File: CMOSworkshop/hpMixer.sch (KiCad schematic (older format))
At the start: 22 parts, among them J1 JACK_STEREO, U4 TL082

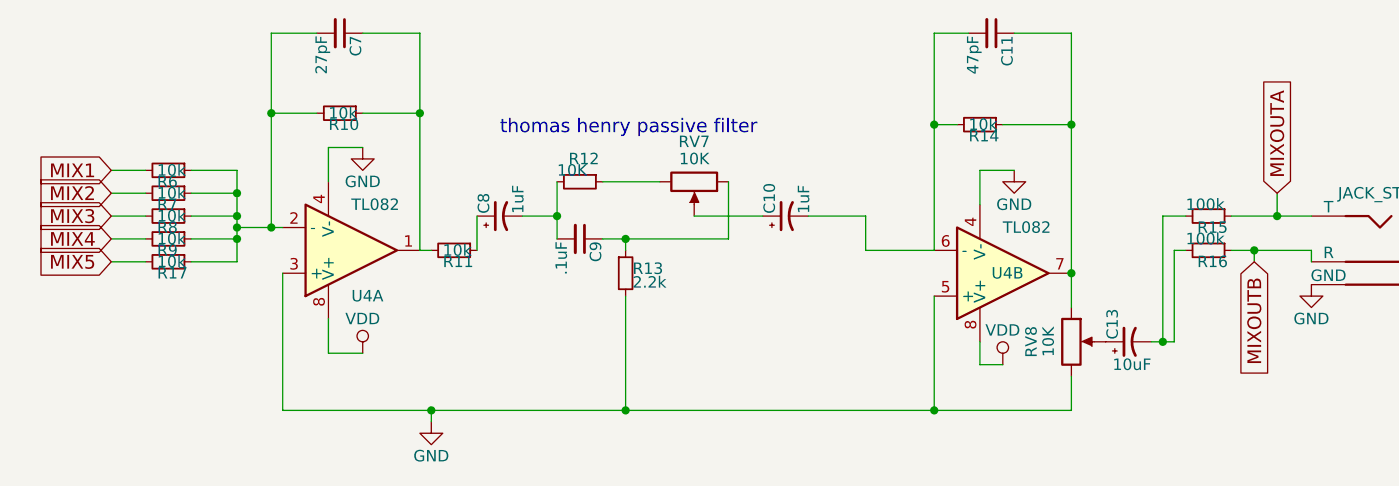
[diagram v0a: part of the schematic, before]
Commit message: updated pcb to accomodate 9v battery and made mixer circuit SMT due to space restrictions.  Spaced out knobs and touchpads for better ergonomics, and created touchpad footprints.
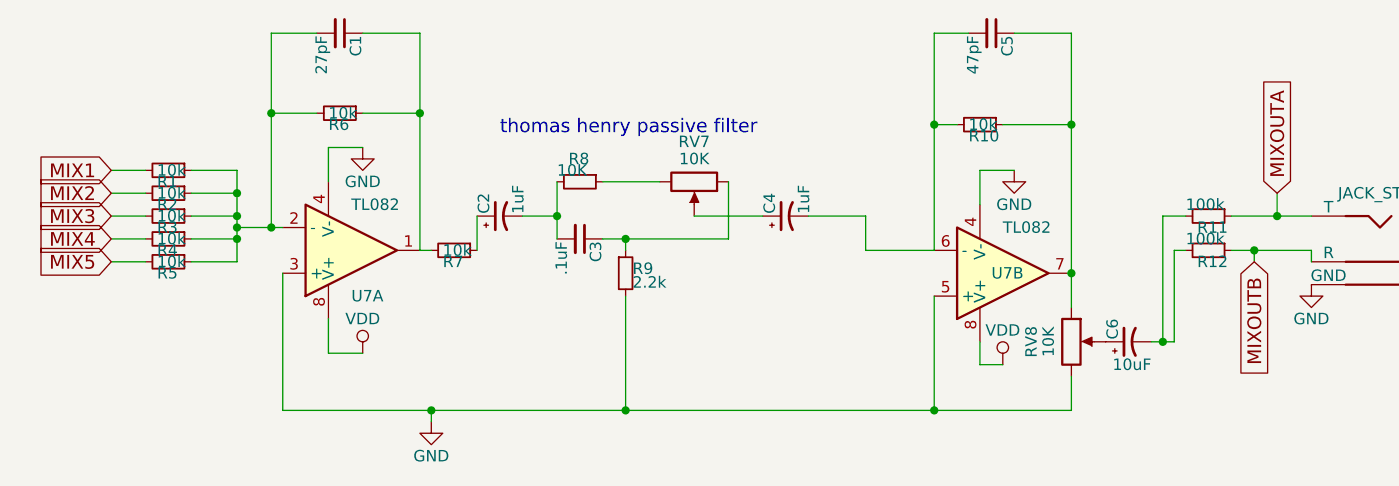
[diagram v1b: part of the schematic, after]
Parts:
- C2: renamed from C8; footprint Capacitors_THT:CP_Radial_D5.0mm_P2.50mm -> Capacitors_ThroughHole:C_Radial_D5_L11_P2.5
- C3: renamed from C9; footprint Capacitors_THT:CP_Radial_D5.0mm_P2.50mm -> Capacitors_THT:C_Rect_L4.0mm_W2.5mm_P2.50mm
- C4: renamed from C10; footprint Capacitors_THT:CP_Radial_D5.0mm_P2.50mm -> Capacitors_ThroughHole:C_Radial_D5_L11_P2.5
- C6: renamed from C13; footprint Capacitors_THT:CP_Radial_D5.0mm_P2.50mm -> Capacitors_ThroughHole:C_Radial_D5_L11_P2.5
- renumbered C7 to C1, C11 to C5, R6 to R1, R14 to R10, R15 to R11, R16 to R12, R7 to R2, R8 to R3, R9 to R4, R17 to R5, R10 to R6, R11 to R7, R12 to R8, R13 to R9, U4 to U7
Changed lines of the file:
@@
 LIBS:contrib
 LIBS:valves
+LIBS:CMOSworkshop-cache
 LIBS:4ms_JST_2x8
 LIBS:4ms-headers
@@
 LIBS:w_microcontrollers
 LIBS:wayne_and_layne_kicad_symbols
-LIBS:74xgxx
-LIBS:ac-dc
-LIBS:actel
-LIBS:allegro
-LIBS:Altera
-LIBS:analog_devices
-LIBS:battery_management
-LIBS:bbd
-LIBS:brooktre
-LIBS:cmos_ieee
-LIBS:dc-dc
-LIBS:diode
-LIBS:elec-unifil
-LIBS:ESD_Protection
-LIBS:ftdi
-LIBS:gennum
-LIBS:graphic
-LIBS:hc11
-LIBS:ir
-LIBS:Lattice
-LIBS:logo
-LIBS:maxim
-LIBS:mechanical
-LIBS:microchip_dspic33dsc
-LIBS:microchip_pic10mcu
-LIBS:microchip_pic12mcu
-LIBS:microchip_pic16mcu
-LIBS:microchip_pic18mcu
-LIBS:microchip_pic32mcu
-LIBS:motor_drivers
-LIBS:motors
-LIBS:msp430
-LIBS:nordicsemi
-LIBS:nxp_armmcu
-LIBS:onsemi
-LIBS:Oscillators
-LIBS:Power_Management
-LIBS:powerint
-LIBS:pspice
-LIBS:references
-LIBS:relays
-LIBS:rfcom
-LIBS:sensors
-LIBS:silabs
-LIBS:stm8
-LIBS:stm32
-LIBS:supertex
-LIBS:switches
-LIBS:transf
-LIBS:ttl_ieee
-LIBS:video
-LIBS:wiznet
-LIBS:Worldsemi
-LIBS:Xicor
-LIBS:zetex
-LIBS:Zilog
-LIBS:CMOSworkshop-cache
+LIBS:CMOSworkshop_ThinStrips-cache
 EELAYER 25 0
 EELAYER END
 $Descr A4 11693 8268
 encoding utf-8
-Sheet 5 7
+Sheet 2 3
 Title ""
 Date ""
@@
 $EndDescr
 $Comp
-L R_Small R9
+L R_Small R4
 U 1 1 589D595B
 P 3550 3250
-F 0 "R9" V 3600 3200 50  0000 L CNN
+F 0 "R4" V 3600 3200 50  0000 L CNN
 F 1 "10k" V 3550 3200 50  0000 L CNN
 F 2 "4ms-footprints:R-TH" H 3550 3250 50  0001 C CNN
@@
 $EndComp
 $Comp
-L R_Small R8
+L R_Small R3
 U 1 1 589D5978
 P 3550 3150
-F 0 "R8" V 3600 3100 50  0000 L CNN
+F 0 "R3" V 3600 3100 50  0000 L CNN
 F 1 "10k" V 3550 3100 50  0000 L CNN
 F 2 "4ms-footprints:R-TH" H 3550 3150 50  0001 C CNN
@@
 $EndComp
 $Comp
-L R_Small R7
+L R_Small R2
 U 1 1 589D5998
 P 3550 3050
-F 0 "R7" V 3600 3000 50  0000 L CNN
+F 0 "R2" V 3600 3000 50  0000 L CNN
 F 1 "10k" V 3550 3000 50  0000 L CNN
 F 2 "4ms-footprints:R-TH" H 3550 3050 50  0001 C CNN
@@
 $EndComp
 $Comp
-L R_Small R6
+L R_Small R1
 U 1 1 589D59BB
 P 3550 2950
-F 0 "R6" V 3600 2900 50  0000 L CNN
+F 0 "R1" V 3600 2900 50  0000 L CNN
 F 1 "10k" V 3550 2900 50  0000 L CNN
 F 2 "4ms-footprints:R-TH" H 3550 2950 50  0001 C CNN
@@
 $EndComp
 $Comp
-L TL082 U4
+L TL082 U7
 U 1 1 589D5A43
 P 4350 3300
-F 0 "U4" H 4350 3500 50  0000 L CNN
+F 0 "U7" H 4350 3500 50  0000 L CNN
 F 1 "TL082" H 4350 3100 50  0000 L CNN
 F 2 "Sockets_DIP:DIP-8__300" H 4350 3300 50  0001 C CNN
@@
 $EndComp
 $Comp
-L TL082 U4
+L TL082 U7
 U 2 1 589D5AC0
 P 7200 3400
-F 0 "U4" H 7150 3400 50  0000 L CNN
+F 0 "U7" H 7150 3400 50  0000 L CNN
 F 1 "TL082" H 7200 3200 50  0000 L CNN
 F 2 "Sockets_DIP:DIP-8__300" H 7200 3400 50  0001 C CNN
@@
 	3300 2950 3450 2950
 $Comp
-L R_Small R11
+L R_Small R7
 U 1 1 589D5D50
 P 4800 3300
-F 0 "R11" V 4850 3250 50  0000 L CNN
+F 0 "R7" V 4850 3250 50  0000 L CNN
 F 1 "10k" V 4800 3250 50  0000 L CNN
 F 2 "4ms-footprints:R-TH" H 4800 3300 50  0001 C CNN
@@
 	6900 4000 6900 3500
 $Comp
-L R_Small R10
+L R_Small R6
 U 1 1 589D5E72
 P 4300 2700
-F 0 "R10" V 4350 2650 50  0000 L CNN
+F 0 "R6" V 4350 2650 50  0000 L CNN
 F 1 "10k" V 4300 2650 50  0000 L CNN
 F 2 "4ms-footprints:R-TH" H 4300 2700 50  0001 C CNN
@@
 $EndComp
 $Comp
-L R_Small R14
+L R_Small R10
 U 1 1 589D5EC3
 P 7100 2750
-F 0 "R14" V 7150 2700 50  0000 L CNN
+F 0 "R10" V 7150 2700 50  0000 L CNN
 F 1 "10k" V 7100 2700 50  0000 L CNN
 F 2 "4ms-footprints:R-TH" H 7100 2750 50  0001 C CNN
@@
 	7500 2350 7500 3550
 $Comp
-L C_Small C7
+L C_Small C1
 U 1 1 589D5FCE
 P 4300 2350
-F 0 "C7" H 4310 2420 50  0000 L CNN
+F 0 "C1" H 4310 2420 50  0000 L CNN
 F 1 "27pF" H 4310 2270 50  0000 L CNN
 F 2 "Capacitors_THT:C_Rect_L4.0mm_W2.5mm_P2.50mm" H 4300 2350 50  0001 C CNN
@@
 $EndComp
 $Comp
-L C_Small C11
+L C_Small C5
 U 1 1 589D6047
 P 7150 2350
-F 0 "C11" H 7160 2420 50  0000 L CNN
+F 0 "C5" H 7160 2420 50  0000 L CNN
 F 1 "47pF" H 7160 2270 50  0000 L CNN
 F 2 "Capacitors_THT:C_Rect_L4.0mm_W2.5mm_P2.50mm" H 7150 2350 50  0001 C CNN
@@
 Connection ~ 4700 4000
 $Comp
-L GND #PWR019
+L GND #PWR03
 U 1 1 589D6232
 P 4400 2850
-F 0 "#PWR019" H 4400 2600 50  0001 C CNN
+F 0 "#PWR03" H 4400 2600 50  0001 C CNN
 F 1 "GND" H 4400 2700 50  0000 C CNN
 F 2 "" H 4400 2850 50  0000 C CNN
@@
 $EndComp
 $Comp
-L GND #PWR020
+L GND #PWR04
 U 1 1 589D626A
 P 7250 2950
-F 0 "#PWR020" H 7250 2700 50  0001 C CNN
+F 0 "#PWR04" H 7250 2700 50  0001 C CNN
 F 1 "GND" H 7250 2800 50  0000 C CNN
 F 2 "" H 7250 2950 50  0000 C CNN
@@
 Connection ~ 6900 4000
 $Comp
-L CP1_Small C13
+L CP1_Small C6
 U 1 1 589D6644
 P 7750 3700
-F 0 "C13" H 7760 3770 50  0000 L CNN
+F 0 "C6" H 7760 3770 50  0000 L CNN
 F 1 "10uF" V 7650 3600 50  0000 L CNN
-F 2 "Capacitors_THT:CP_Radial_D5.0mm_P2.50mm" H 7750 3700 50  0001 C CNN
+F 2 "Capacitors_ThroughHole:C_Radial_D5_L11_P2.5" H 7750 3700 50  0001 C CNN
 F 3 "" H 7750 3700 50  0000 C CNN
 	1    7750 3700
@@
 	8200 3300 8550 3300
 $Comp
-L R_Small R15
+L R_Small R11
 U 1 1 589D67E2
 P 8100 3150
-F 0 "R15" V 8150 3100 50  0000 L CNN
+F 0 "R11" V 8150 3100 50  0000 L CNN
 F 1 "100k" V 8050 3050 50  0000 L CNN
 F 2 "4ms-footprints:R-TH" H 8100 3150 50  0001 C CNN
@@
 $EndComp
 $Comp
-L R_Small R16
+L R_Small R12
 U 1 1 589D68B8
 P 8100 3300
-F 0 "R16" V 8150 3250 50  0000 L CNN
+F 0 "R12" V 8150 3250 50  0000 L CNN
 F 1 "100k" V 8050 3200 50  0000 L CNN
 F 2 "4ms-footprints:R-TH" H 8100 3300 50  0001 C CNN
@@
 	3850 2950 3850 3350
 $Comp
-L CP1_Small C8
+L CP1_Small C2
 U 1 1 58A27D1D
 P 5000 3150
-F 0 "C8" H 5010 3220 50  0000 L CNN
+F 0 "C2" H 5010 3220 50  0000 L CNN
 F 1 "1uF" H 5010 3070 50  0000 L CNN
-F 2 "Capacitors_THT:CP_Radial_D5.0mm_P2.50mm" H 5000 3150 50  0001 C CNN
+F 2 "Capacitors_ThroughHole:C_Radial_D5_L11_P2.5" H 5000 3150 50  0001 C CNN
 F 3 "" H 5000 3150 50  0000 C CNN
 	1    5000 3150
@@
 $EndComp
 $Comp
-L R_Small R12
+L R_Small R8
 U 1 1 58A27DDA
 P 5350 3000
-F 0 "R12" V 5250 2950 50  0000 L CNN
+F 0 "R8" V 5250 2950 50  0000 L CNN
 F 1 "10K" V 5300 2900 50  0000 L CNN
 F 2 "4ms-footprints:R-TH" H 5350 3000 50  0001 C CNN
@@
 $EndComp
 $Comp
-L C_Small C9
+L C_Small C3
 U 1 1 58A27E7C
 P 5350 3250
-F 0 "C9" H 5360 3320 50  0000 L CNN
+F 0 "C3" H 5360 3320 50  0000 L CNN
 F 1 ".1uF" H 5360 3170 50  0000 L CNN
-F 2 "Capacitors_THT:CP_Radial_D5.0mm_P2.50mm" H 5350 3250 50  0001 C CNN
+F 2 "Capacitors_THT:C_Rect_L4.0mm_W2.5mm_P2.50mm" H 5350 3250 50  0001 C CNN
 F 3 "" H 5350 3250 50  0000 C CNN
 	1    5350 3250
@@
 $EndComp
 $Comp
-L R_Small R13
+L R_Small R9
 U 1 1 58A27F28
 P 5550 3400
-F 0 "R13" H 5580 3420 50  0000 L CNN
+F 0 "R9" H 5580 3420 50  0000 L CNN
 F 1 "2.2k" H 5580 3360 50  0000 L CNN
 F 2 "4ms-footprints:R-TH" H 5550 3400 50  0001 C CNN
@@
 	5550 3500 5550 4000
 $Comp
-L CP1_Small C10
+L CP1_Small C4
 U 1 1 58A28220
 P 6250 3150
-F 0 "C10" H 6260 3220 50  0000 L CNN
+F 0 "C4" H 6260 3220 50  0000 L CNN
 F 1 "1uF" H 6260 3070 50  0000 L CNN
-F 2 "Capacitors_THT:CP_Radial_D5.0mm_P2.50mm" H 6250 3150 50  0001 C CNN
+F 2 "Capacitors_ThroughHole:C_Radial_D5_L11_P2.5" H 6250 3150 50  0001 C CNN
 F 3 "" H 6250 3150 50  0000 C CNN
 	1    6250 3150
@@
 thomas henry passive filter\n
 $Comp
-L VDD #PWR021
+L VDD #PWR05
 U 1 1 58A517E6
 P 4400 3750
-F 0 "#PWR021" H 4400 3600 50  0001 C CNN
+F 0 "#PWR05" H 4400 3600 50  0001 C CNN
 F 1 "VDD" H 4400 3900 50  0000 C CNN
 F 2 "" H 4400 3750 50  0000 C CNN
@@
 	4250 3750 4400 3750
 $Comp
-L VDD #PWR022
+L VDD #PWR06
 U 1 1 58A51896
 P 7200 3800
-F 0 "#PWR022" H 7200 3650 50  0001 C CNN
+F 0 "#PWR06" H 7200 3650 50  0001 C CNN
 F 1 "VDD" H 7200 3950 50  0000 C CNN
 F 2 "" H 7200 3800 50  0000 C CNN
@@
 MIX1
 $Comp
-L R_Small R17
+L R_Small R5
 U 1 1 58A53865
 P 3550 3350
-F 0 "R17" V 3600 3300 50  0000 L CNN
+F 0 "R5" V 3600 3300 50  0000 L CNN
 F 1 "10k" V 3550 3300 50  0000 L CNN
 F 2 "4ms-footprints:R-TH" H 3550 3350 50  0001 C CNN
@@
 $EndComp
 $Comp
-L GND #PWR023
+L GND #PWR07
 U 1 1 58A907F0
 P 4700 4050
-F 0 "#PWR023" H 4700 3800 50  0001 C CNN
+F 0 "#PWR07" H 4700 3800 50  0001 C CNN
 F 1 "GND" H 4700 3900 50  0000 C CNN
 F 2 "" H 4700 4050 50  0000 C CNN
@@
 	8550 3300 8550 3350
 $Comp
-L GND #PWR024
+L GND #PWR08
 U 1 1 58A90EFF
 P 8550 3450
-F 0 "#PWR024" H 8550 3200 50  0001 C CNN
+F 0 "#PWR08" H 8550 3200 50  0001 C CNN
 F 1 "GND" H 8550 3300 50  0000 C CNN
 F 2 "" H 8550 3450 50  0000 C CNN

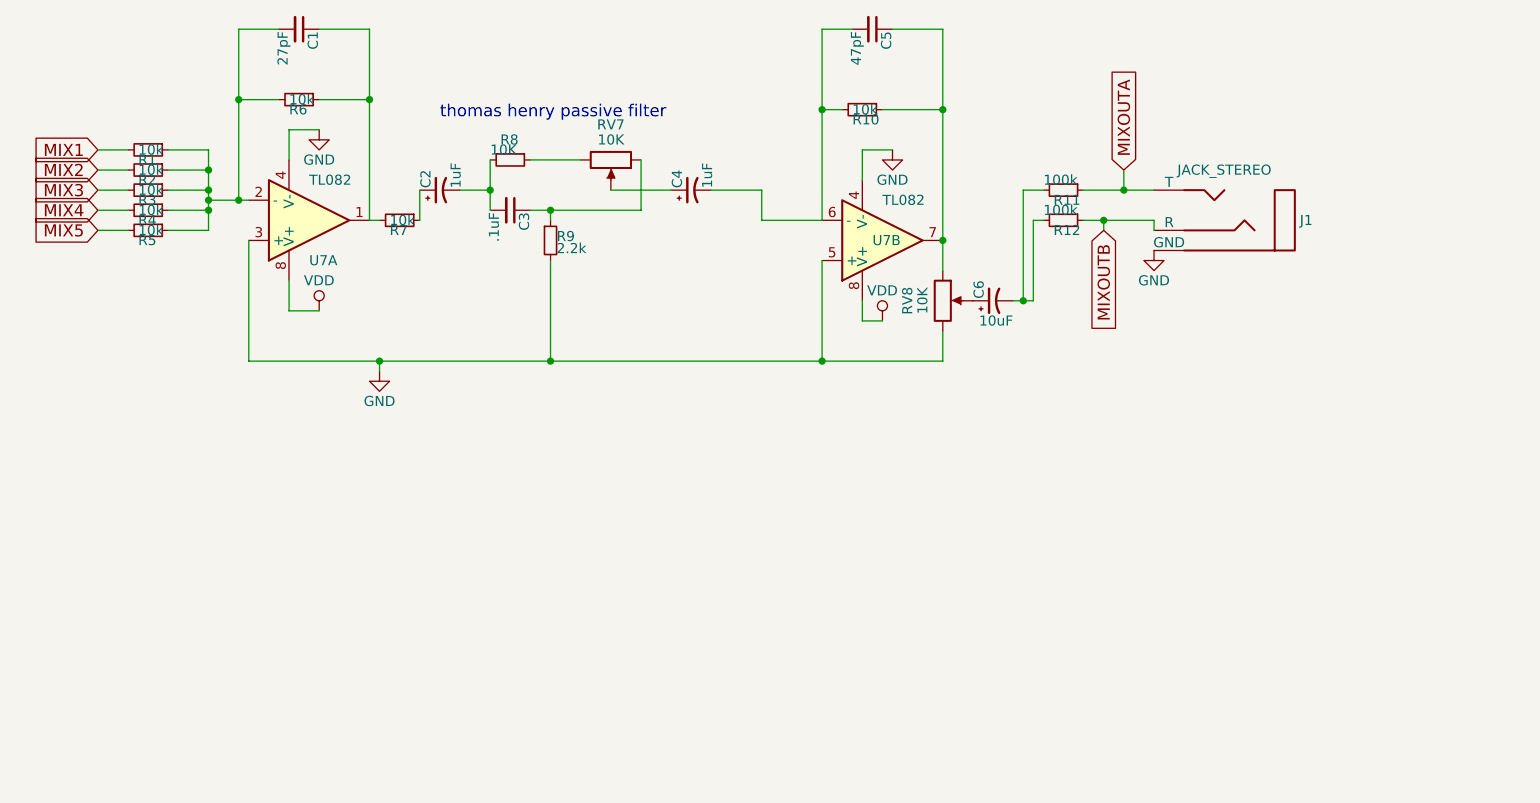
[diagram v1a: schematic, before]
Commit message: updated mixer schematic, added 9v battery holder and laid out components.
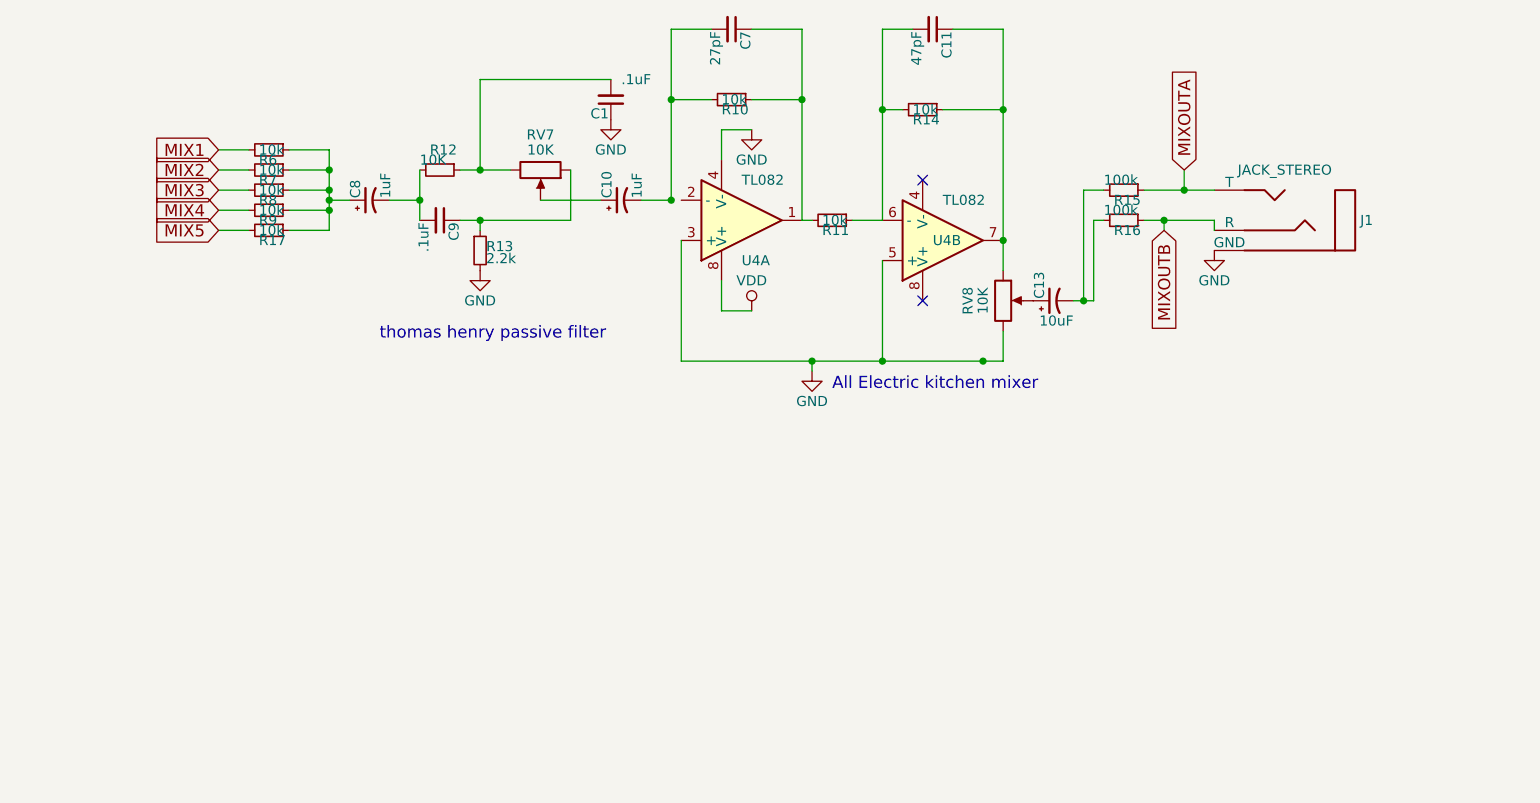
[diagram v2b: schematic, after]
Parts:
- added C1: .1uF, Capacitors_THT:CP_Radial_D5.0mm_P2.50mm, symbol C_Small
- C10: renamed from C4; footprint Capacitors_ThroughHole:C_Radial_D5_L11_P2.5 -> Capacitors_THT:CP_Radial_D5.0mm_P2.50mm
- C13: renamed from C6; footprint Capacitors_ThroughHole:C_Radial_D5_L11_P2.5 -> Capacitors_THT:CP_Radial_D5.0mm_P2.50mm
- C8: renamed from C2; footprint Capacitors_ThroughHole:C_Radial_D5_L11_P2.5 -> Capacitors_THT:CP_Radial_D5.0mm_P2.50mm
- C9: renamed from C3; footprint Capacitors_THT:C_Rect_L4.0mm_W2.5mm_P2.50mm -> Capacitors_THT:CP_Radial_D5.0mm_P2.50mm
- renumbered C5 to C11, C1 to C7, R6 to R10, R7 to R11, R8 to R12, R9 to R13, R10 to R14, R11 to R15, R12 to R16, R5 to R17, R1 to R6, R2 to R7, R3 to R8, R4 to R9, U7 to U4
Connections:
- net GND: now also C1.1; no longer U4.4 (V-)
- net VDD: no longer U4.8 (V+)
- net at R17.1, R6.1, R7.1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: now also C8.+; no longer C7.2, R10.2, U4.2 (-)
- net at C11.2, R14.2, U4.6 (-): now also R11.1; no longer C10.-
- net at R12.1, RV7.3: now also C1.2
- new net: C10.-, C7.2, R10.2
- no-connect marks 0 -> 2
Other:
- note added: "All Electric kitchen mixer\n"
- moved on the sheet: C10, C11, C13, C7, C8, C9, J1, R10, R11, R12, R13, R14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

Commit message: added traces for mixer circuit and made small connection in hp mixer
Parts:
- C10, C13, C8: symbol CP1_Small -> CP1_Small-RESCUE-CMOSworkshop_ThinStrips
- R10, R11, R12, R13, R14, R15, R16, R17, R6, R7, R8, R9: symbol R_Small -> R_Small-RESCUE-CMOSworkshop_ThinStrips
- RV7, RV8: symbol POT -> POT-RESCUE-CMOSworkshop_ThinStrips
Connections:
- net at U4.2 (-): now also C10.-, C7.2, R10.2
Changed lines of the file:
@@
 EESchema Schematic File Version 2
+LIBS:CMOSworkshop_ThinStrips-rescue
 LIBS:power
 LIBS:device
@@
 LIBS:valves
 LIBS:CMOSworkshop-cache
-LIBS:4ms_JST_2x8
-LIBS:4ms-headers
-LIBS:4ms-ic
-LIBS:4ms-mech
-LIBS:4ms-passives
-LIBS:4ms-power
-LIBS:AudioBoardLib
-LIBS:EtherkitKicadLibrary
-LIBS:lm4880m
-LIBS:max97220
-LIBS:STM32F429_LQFP144
-LIBS:tpa6130
-LIBS:w_microcontrollers
-LIBS:wayne_and_layne_kicad_symbols
 LIBS:CMOSworkshop_ThinStrips-cache
 EELAYER 25 0
@@
 $EndDescr
 $Comp
-L R_Small R9
+L R_Small-RESCUE-CMOSworkshop_ThinStrips R9
 U 1 1 589D595B
 P 4150 3250
@@
 $EndComp
 $Comp
-L R_Small R8
+L R_Small-RESCUE-CMOSworkshop_ThinStrips R8
 U 1 1 589D5978
 P 4150 3150
@@
 $EndComp
 $Comp
-L R_Small R7
+L R_Small-RESCUE-CMOSworkshop_ThinStrips R7
 U 1 1 589D5998
 P 4150 3050
@@
 $EndComp
 $Comp
-L R_Small R6
+L R_Small-RESCUE-CMOSworkshop_ThinStrips R6
 U 1 1 589D59BB
 P 4150 2950
@@
 	3900 2950 4050 2950
 $Comp
-L R_Small R11
+L R_Small-RESCUE-CMOSworkshop_ThinStrips R11
 U 1 1 589D5D50
 P 6950 3300
@@
 	7200 4000 7200 3500
 $Comp
-L R_Small R10
+L R_Small-RESCUE-CMOSworkshop_ThinStrips R10
 U 1 1 589D5E72
 P 6450 2700
@@
 $EndComp
 $Comp
-L R_Small R14
+L R_Small-RESCUE-CMOSworkshop_ThinStrips R14
 U 1 1 589D5EC3
 P 7400 2750
@@
 	6400 2850 6400 3000
 $Comp
-L POT RV8
+L POT-RESCUE-CMOSworkshop_ThinStrips RV8
 U 1 1 589D644C
 P 7800 3700
@@
 Connection ~ 7200 4000
 $Comp
-L CP1_Small C13
+L CP1_Small-RESCUE-CMOSworkshop_ThinStrips C13
 U 1 1 589D6644
 P 8050 3700
+AR Path="/589D6644" Ref="C13"  Part="1"
+AR Path="/589D4DD6/589D6644" Ref="C13"  Part="1"
 F 0 "C13" H 8060 3770 50  0000 L CNN
 F 1 "10uF" V 7950 3600 50  0000 L CNN
@@
 	8500 3300 8850 3300
 $Comp
-L R_Small R15
+L R_Small-RESCUE-CMOSworkshop_ThinStrips R15
 U 1 1 589D67E2
 P 8400 3150
@@
 $EndComp
 $Comp
-L R_Small R16
+L R_Small-RESCUE-CMOSworkshop_ThinStrips R16
 U 1 1 589D68B8
 P 8400 3300
@@
 	4450 2950 4450 3350
 $Comp
-L CP1_Small C8
+L CP1_Small-RESCUE-CMOSworkshop_ThinStrips C8
 U 1 1 58A27D1D
 P 4650 3200
+AR Path="/58A27D1D" Ref="C8"  Part="1"
+AR Path="/589D4DD6/58A27D1D" Ref="C8"  Part="1"
 F 0 "C8" H 4660 3270 50  0000 L CNN
 F 1 "1uF" H 4660 3120 50  0000 L CNN
@@
 $EndComp
 $Comp
-L R_Small R12
+L R_Small-RESCUE-CMOSworkshop_ThinStrips R12
 U 1 1 58A27DDA
 P 5000 3050
@@
 $EndComp
 $Comp
-L R_Small R13
+L R_Small-RESCUE-CMOSworkshop_ThinStrips R13
 U 1 1 58A27F28
 P 5200 3450
@@
 $EndComp
 $Comp
-L POT RV7
+L POT-RESCUE-CMOSworkshop_ThinStrips RV7
 U 1 1 58A28022
 P 5500 3050
@@
 	5200 3300 5200 3350
 $Comp
-L CP1_Small C10
+L CP1_Small-RESCUE-CMOSworkshop_ThinStrips C10
 U 1 1 58A28220
 P 5900 3200
+AR Path="/58A28220" Ref="C10"  Part="1"
+AR Path="/589D4DD6/58A28220" Ref="C10"  Part="1"
 F 0 "C10" H 5910 3270 50  0000 L CNN
 F 1 "1uF" H 5910 3120 50  0000 L CNN
@@
 MIX1
 $Comp
-L R_Small R17
+L R_Small-RESCUE-CMOSworkshop_ThinStrips R17
 U 1 1 58A53865
 P 4150 3350
@@
 NoConn ~ 7400 3100
 Wire Wire Line
-	6150 3200 6000 3200
+	6000 3200 6200 3200
 Text Notes 6950 4150 0    60   ~ 0
 All Electric kitchen mixer\n
